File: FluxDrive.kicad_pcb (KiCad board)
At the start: 4 copper layers, 60 x 54.5 mm, 124 parts, among them J1 Amiga floppy 34, J2 Floppy power, J3 USB-C, J4 UART / recovery, J5 Spare GPIO, SW1 BOOT, SW2 RESET, U1 ESP32-S3-WROOM-1-N16R8, U2 74LVC14A, U3 74LVC14A, U4 74LVC07A, U5 TPS259531, U6 TLV62569DBVR, U7 USBLC6-2SC6

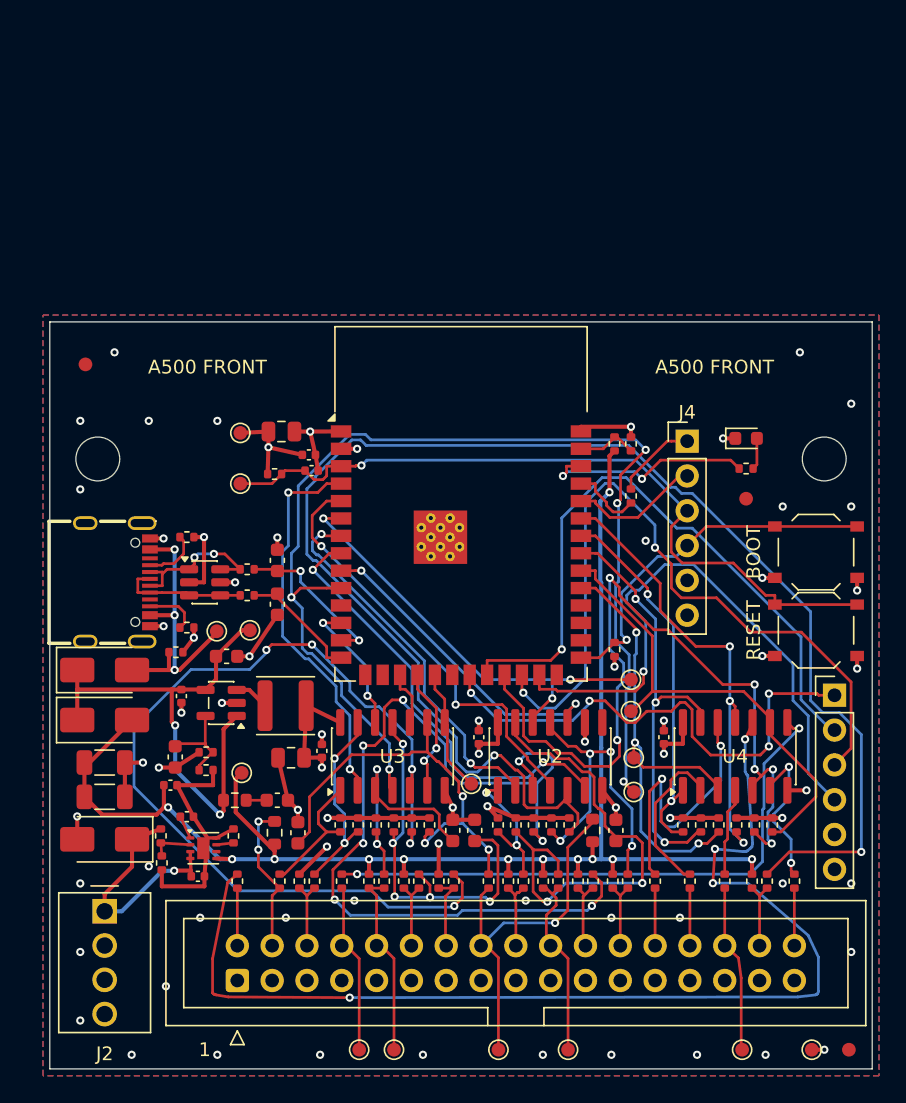
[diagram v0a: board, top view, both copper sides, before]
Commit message: Rev B placement: J6 beside J1, 72.1 mm, every part found by net (unrouted)
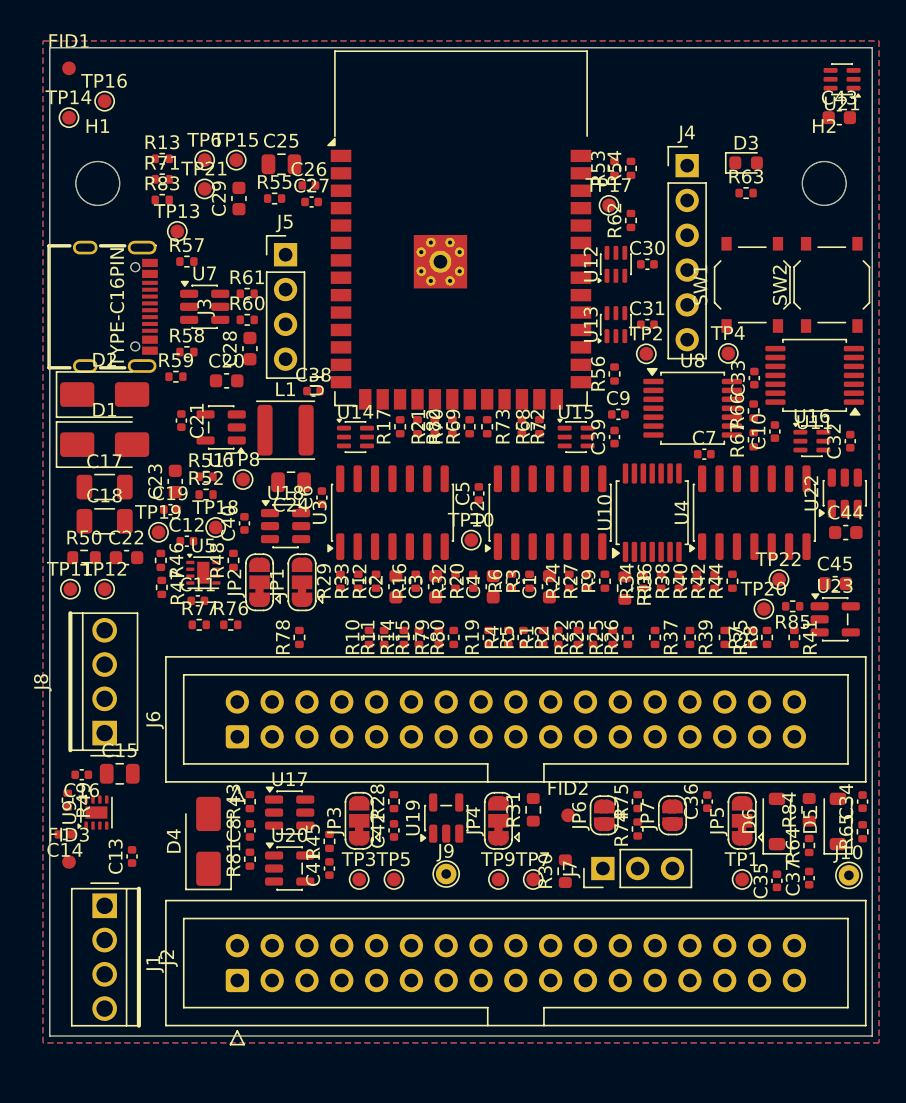
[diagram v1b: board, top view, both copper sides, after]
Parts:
- added C23: 15pF, Capacitor_SMD:C_0603_1608Metric, F.Cu at (109.2, 105.1)
- added C24: 22uF, Capacitor_SMD:C_0805_2012Metric, F.Cu at (117.6, 105.2)
- added C25: 22uF, Capacitor_SMD:C_0805_2012Metric, F.Cu at (116.9, 82.0)
- added C26: 100nF, Capacitor_SMD:C_0402_1005Metric, F.Cu at (118.9, 83.5)
- added C27: 1uF, Capacitor_SMD:C_0402_1005Metric, F.Cu at (119.1, 84.8)
- added C28: 10pF, Capacitor_SMD:C_0603_1608Metric, F.Cu at (114.6, 95.5)
- added C29: 10pF, Capacitor_SMD:C_0603_1608Metric, F.Cu at (113.8, 84.5)
- added C30: 100nF, Capacitor_SMD:C_0402_1005Metric, F.Cu at (143.6, 89.3)
- added C31: 100nF, Capacitor_SMD:C_0402_1005Metric, F.Cu at (143.6, 93.7)
- added C32: 100nF, Capacitor_SMD:C_0402_1005Metric, F.Cu at (158.4, 102.2)
- added C33: 100nF, Capacitor_SMD:C_0402_1005Metric, F.Cu at (151.4, 97.6)
- added C34: 1uF, Capacitor_SMD:C_0402_1005Metric, F.Cu at (159.3, 128.5)
- added C35: 1uF, Capacitor_SMD:C_0402_1005Metric, F.Cu at (153.1, 134.3)
- added C36: 100nF, Capacitor_SMD:C_0402_1005Metric, F.Cu at (148.0, 128.5)
- added C37: 100nF, Capacitor_SMD:C_0402_1005Metric, F.Cu at (155.4, 134.1)
- added C38: 100nF, Capacitor_SMD:C_0402_1005Metric, F.Cu at (119.2, 98.5)
- added C39: 100nF, Capacitor_SMD:C_0402_1005Metric, F.Cu at (141.2, 101.9)
- added C40: 100nF, Capacitor_SMD:C_0402_1005Metric, F.Cu at (114.2, 108.2)
- added C41: 100nF, Capacitor_SMD:C_0402_1005Metric, F.Cu at (120.4, 133.4)
- added C42: 100nF, Capacitor_SMD:C_0402_1005Metric, F.Cu at (125.1, 130.6)
- added C43: 100nF, Capacitor_SMD:C_0603_1608Metric, F.Cu at (157.6, 78.6)
- added C44: 100nF, Capacitor_SMD:C_0603_1608Metric, F.Cu at (158.1, 108.9)
- added C45: 100nF, Capacitor_SMD:C_0603_1608Metric, F.Cu at (157.3, 112.6)
- added D5: 1N4148W, Diode_SMD:D_SOD-123, F.Cu at (157.5, 129.9)
- added D6: 1N4148W, Diode_SMD:D_SOD-123, F.Cu at (153.1, 129.9)
- added J10: MTRX wire, TestPoint:TestPoint_THTPad_D1.5mm_Drill0.7mm, F.Cu at (158.3, 133.9)
- added J6: Original drive, Connector_IDC:IDC-Header_2x17_P2.54mm_Vertical, F.Cu at (113.7, 123.8)
- added J7: DF0 switch, Connector_PinHeader_2.54mm:PinHeader_1x03_P2.54mm_Vertical, F.Cu at (140.3, 133.4)
- added J8: Drive power, FluxDrive:171825-4, F.Cu at (104.0, 123.5)
- added J9: RST wire, TestPoint:TestPoint_THTPad_D1.5mm_Drill0.7mm, F.Cu at (128.9, 133.8)
- added JP1: bypass SEL, Jumper:SolderJumper-3_P1.3mm_Bridged12_RoundedPad1.0x1.5mm, F.Cu at (118.4, 112.5)
- added JP2: bypass MTR, Jumper:SolderJumper-3_P1.3mm_Bridged12_RoundedPad1.0x1.5mm, F.Cu at (115.3, 112.5)
- added JP3: mode 4 SEL, Jumper:SolderJumper-3_P1.3mm_Bridged12_RoundedPad1.0x1.5mm, F.Cu at (122.6, 129.9)
- added JP4: mode 4 MTR, Jumper:SolderJumper-3_P1.3mm_Bridged12_RoundedPad1.0x1.5mm, F.Cu at (132.7, 129.9)
- added JP5: DF0 at power-on, Jumper:SolderJumper-3_P1.3mm_Bridged12_RoundedPad1.0x1.5mm, F.Cu at (150.5, 129.9)
- added JP6: REAL clear, Jumper:SolderJumper-2_P1.3mm_Open_RoundedPad1.0x1.5mm, F.Cu at (140.4, 129.5)
- added JP7: REAL preset, Jumper:SolderJumper-2_P1.3mm_Open_RoundedPad1.0x1.5mm, F.Cu at (145.4, 129.5)
- added R63: 1K, Resistor_SMD:R_0402_1005Metric, F.Cu at (150.8, 84.1)
- added R64: 10K, Resistor_SMD:R_0402_1005Metric, F.Cu at (155.4, 131.7)
- added R65: 10K, Resistor_SMD:R_0402_1005Metric, F.Cu at (159.3, 130.7)
- added R66: 10K, Resistor_SMD:R_0402_1005Metric, F.Cu at (151.3, 100.0)
- added R67: 10K, Resistor_SMD:R_0402_1005Metric, F.Cu at (151.3, 102.1)
- added R68: 100K, Resistor_SMD:R_0402_1005Metric, F.Cu at (135.7, 101.2)
- added R69: 100K, Resistor_SMD:R_0402_1005Metric, F.Cu at (130.6, 101.2)
- added R70: 1K, Resistor_SMD:R_0402_1005Metric, F.Cu at (129.4, 101.2)
- added R71: 1K, Resistor_SMD:R_0402_1005Metric, F.Cu at (108.2, 83.1)
- added R72: 10K, Resistor_SMD:R_0402_1005Metric, F.Cu at (134.4, 101.2)
- added R73: 10K, Resistor_SMD:R_0402_1005Metric, F.Cu at (131.9, 101.2)
- added R74: 1K, Resistor_SMD:R_0402_1005Metric, F.Cu at (142.9, 130.5)
- added R75: 1K, Resistor_SMD:R_0402_1005Metric, F.Cu at (142.9, 128.5)
- added R76: 4K7, Resistor_SMD:R_0402_1005Metric, F.Cu at (113.2, 115.6)
- added R77: 4K7, Resistor_SMD:R_0402_1005Metric, F.Cu at (110.9, 115.6)
- added R78: 10K, Resistor_SMD:R_0402_1005Metric, F.Cu at (118.2, 116.5)
- added R79: 10K, Resistor_SMD:R_0402_1005Metric, F.Cu at (128.4, 116.5)
- added R80: 10K, Resistor_SMD:R_0402_1005Metric, F.Cu at (129.5, 116.5)
- added R81: 33, Resistor_SMD:R_0402_1005Metric, F.Cu at (114.6, 132.7)
- added R82: 10K, Resistor_SMD:R_0402_1005Metric, F.Cu at (126.8, 101.2)
- added R83: 1K, Resistor_SMD:R_0402_1005Metric, F.Cu at (108.2, 84.6)
- added R84: 33, Resistor_SMD:R_0603_1608Metric, F.Cu at (155.4, 129.1)
- added R85: 100K, Resistor_SMD:R_0402_1005Metric, F.Cu at (154.2, 114.2)
- added TP17: SEL_FD, TestPoint:TestPoint_Pad_D1.0mm, F.Cu at (140.8, 85.0)
- added TP18: REAL_SEL, TestPoint:TestPoint_Pad_D1.0mm, F.Cu at (112.1, 108.5)
- added TP19: REAL_MTR, TestPoint:TestPoint_Pad_D1.0mm, F.Cu at (107.9, 108.8)
- added TP20: DF0_FD, TestPoint:TestPoint_Pad_D1.0mm, F.Cu at (152.1, 114.5)
- added TP21: DF1_EN, TestPoint:TestPoint_Pad_D1.0mm, F.Cu at (111.3, 83.8)
- added TP22: MODE_CLK, TestPoint:TestPoint_Pad_D1.0mm, F.Cu at (153.2, 112.3)
- added U10: 74LVC32A, Package_SO:TSSOP-14_4.4x5mm_P0.65mm, F.Cu at (143.9, 107.4)
- added U11: 74LVC32A, Package_SO:TSSOP-14_4.4x5mm_P0.65mm, F.Cu at (155.8, 97.4)
- added U12: 74LVC1G157, Package_TO_SOT_SMD:SOT-363_SC-70-6, F.Cu at (141.3, 89.3)
- added U13: 74LVC1G157, Package_TO_SOT_SMD:SOT-363_SC-70-6, F.Cu at (141.3, 93.7)
- added U14: 74LVC1G157, Package_TO_SOT_SMD:SOT-363_SC-70-6, F.Cu at (122.3, 101.9)
- added U15: 74LVC1G157, Package_TO_SOT_SMD:SOT-363_SC-70-6, F.Cu at (138.4, 101.9)
- added U16: 74LVC1G157, Package_TO_SOT_SMD:SOT-363_SC-70-6, F.Cu at (155.6, 102.2)
- added U17: SN74LVC2G07, Package_TO_SOT_SMD:SOT-23-6, F.Cu at (117.5, 129.3)
- added U18: SN74LVC2G06, Package_TO_SOT_SMD:SOT-23-6, F.Cu at (117.2, 108.4)
- added U19: SN74LVC1G06, Package_TO_SOT_SMD:SOT-23-5, F.Cu at (128.9, 129.7)
- added U20: SN74LVC1G38, Package_TO_SOT_SMD:SOT-23-5, F.Cu at (117.5, 133.4)
- added U21: 74LVC1G157, Package_TO_SOT_SMD:SOT-363_SC-70-6, F.Cu at (157.8, 75.8)
- added U22: SN74LVC1G175, Package_TO_SOT_SMD:SOT-23-6, F.Cu at (158.0, 106.0)
- added U23: SN74LVC1G38, Package_TO_SOT_SMD:SOT-23-5, F.Cu at (157.3, 115.2)
- added U8: 74LVC74A, Package_SO:TSSOP-14_4.4x5mm_P0.65mm, F.Cu at (146.9, 99.8)
- added U9: TPS259531, Package_SON:Texas_DSG0008A_WSON-8-1EP_2x2mm_P0.5mm_EP0.9x1.6mm, F.Cu at (103.4, 129.3)
- C10: value 47uF -> 100nF; footprint Capacitor_SMD:C_1206_3216Metric -> Capacitor_SMD:C_0402_1005Metric
- C11: value 47uF -> 1uF; footprint Capacitor_SMD:C_1206_3216Metric -> Capacitor_SMD:C_0402_1005Metric
- C12, C14: value 100nF -> 22nF
- C13: value 10uF -> 1uF; footprint Capacitor_SMD:C_0603_1608Metric -> Capacitor_SMD:C_0402_1005Metric
- C15: value 4.7uF -> 22uF; footprint Capacitor_SMD:C_0603_1608Metric -> Capacitor_SMD:C_0805_2012Metric
- C16: value 15pF -> 100nF; footprint Capacitor_SMD:C_0603_1608Metric -> Capacitor_SMD:C_0402_1005Metric
- C17, C18: value 22uF -> 47uF; footprint Capacitor_SMD:C_0805_2012Metric -> Capacitor_SMD:C_1206_3216Metric
- C20: value 1uF -> 10uF; footprint Capacitor_SMD:C_0402_1005Metric -> Capacitor_SMD:C_0603_1608Metric
- C21: value 10pF -> 100nF; footprint Capacitor_SMD:C_0603_1608Metric -> Capacitor_SMD:C_0402_1005Metric
- C22: value 10pF -> 4.7uF
- C8: value 1uF -> 100nF
- C9: value 22nF -> 100nF
- J5: value Spare GPIO -> Spare / OLED; footprint Connector_PinHeader_2.54mm:PinHeader_1x06_P2.54mm_Vertical -> Connector_PinHeader_2.54mm:PinHeader_1x04_P2.54mm_Vertical
- R1, R4, R7: value 1K -> 4K7
- R13: value 10K -> 1K
- R14, R17: value 100 -> 1K
- R15: value 100K -> 100
- R16: value 1K -> 100K; footprint Resistor_SMD:R_0603_1608Metric -> Resistor_SMD:R_0402_1005Metric
- R18: value 100K -> 1K; footprint Resistor_SMD:R_0402_1005Metric -> Resistor_SMD:R_0603_1608Metric
- R19: value 4K7 -> 100
- R20, R29, R32: value 100 -> 100K
- R21: value 100K -> 1K
- R25: value 1K -> 4K7; footprint Resistor_SMD:R_0603_1608Metric -> Resistor_SMD:R_0402_1005Metric
- R28: value 10K -> 100
- R30: value 100K -> 4K7; footprint Resistor_SMD:R_0402_1005Metric -> Resistor_SMD:R_0603_1608Metric
- R31: value 10K -> 100; footprint Resistor_SMD:R_0402_1005Metric -> Resistor_SMD:R_0603_1608Metric
- R49: value 1R -> 1K37; footprint Resistor_SMD:R_0603_1608Metric -> Resistor_SMD:R_0402_1005Metric
- R50: value 100K -> 1R; footprint Resistor_SMD:R_0402_1005Metric -> Resistor_SMD:R_0603_1608Metric
- R51: value 22K -> 100K
- R52: value 1K -> 22K
- R53: value 1K5 -> 1K
- R54: value 10K -> 1K5
- R56: value 5K1 -> 10K
- R58: value 10K -> 5K1
- R59: value 22 -> 10K
- R61: value 470 -> 22
- R62: value 1K -> 470
- moved TP16 86.3 mm to (104.0, 77.4)
- moved FID3 58.5 mm to (101.4, 132.9)
- moved TP6 55.7 mm to (111.3, 81.7)
- moved R13 55.6 mm to (108.2, 81.6), turned to 0 degrees
- moved C10 54.5 mm to (152.9, 101.5), turned to 90 degrees
- moved J5 51.4 mm to (117.2, 88.6)
- moved C9 43.0 mm to (141.5, 100.2)
- moved R55 41.2 mm to (116.4, 84.5), turned to 0 degrees
- moved R54 34.3 mm to (142.4, 82.3), turned to 90 degrees
- moved R45 34.0 mm to (120.4, 131.4), turned to 90 degrees
- moved R17 33.8 mm to (125.6, 101.2)
- moved R56 33.4 mm to (141.2, 97.3), turned to 90 degrees
- moved TP8 31.8 mm to (114.1, 105.0)
- moved R61 31.6 mm to (114.4, 91.5), turned to 0 degrees
- moved R26 31.0 mm to (142.2, 116.5)
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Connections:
- C10 pad 1: /+5V_A -> /+3V3
- C11 pad 1: /+5V_A -> /+5V_IN
- C12 pad 1: /+5V_A -> /EFUSE_DVDT
- C13 pad 1: /V5SYS -> /+5V_IN
- C14 pad 1: /V5SYS -> /DRV_DVDT
- C15 pad 1: /V5SYS_DAMP -> /+5V_DRIVE
- C16 pad 1: /+3V3 -> /+5V_DRIVE
- C16 pad 2: /BUCK_FB -> /GND
- C17 pad 1: /+3V3 -> /+5V_A
- C18 pad 1: /+3V3 -> /+5V_A
- C19 pad 1: /+3V3 -> /+5V_A
- C20 pad 1: /ESP_EN -> /V5SYS
- C21 pad 1: /USB_DP -> /V5SYS
- C22 pad 1: /USB_DN -> /V5SYS_DAMP
- C8 pad 1: /+5V_IN -> /+3V3
- C9 pad 1: /EFUSE_DVDT -> /+3V3
- J1 pad 14: /FD_PIN14 -> unconnected-(J1-Pin_14-Pad14)
- J1 pad 4: /_MTR0_P4 -> unconnected-(J1-Pin_4-Pad4)
- J1 pad 6: /FD_PIN6 -> unconnected-(J1-Pin_6-Pad6)
- J2 pad 4: unconnected-(J2-12V-Pad4) -> /+12V
- J5 pad 1: /GPIO13 -> /GND
- J5 pad 2: /GPIO14 -> /+3V3
- J5 pad 3: /GPIO47 -> /GPIO18
- J5 pad 4: /GPIO48 -> /GPIO3
- R13 pad 1: /_SEL1 -> /SEL0
- R13 pad 2: /+5V_A -> /SEL0_IO
- R14 pad 2: /SEL1_B -> /+5V_A
- R15 pad 1: /SEL1_B -> /_SEL1
- R15 pad 2: /+3V3 -> /SEL1_B
- R16 pad 1: /_MTR0 -> /SEL1_B
- R16 pad 2: /+5V_A -> /+3V3
- R17 pad 1: /_MTR0 -> /SEL1
- R17 pad 2: /MTR0_B -> /SEL1_IO
- R18 pad 1: /MTR0_B -> /_MTR0
- R18 pad 2: /+3V3 -> /+5V_A
- R19 pad 1: /_DKWD -> /_MTR0
- R19 pad 2: /+5V_A -> /MTR0_B
- R20 pad 1: /_DKWD -> /MTR0_B
- R20 pad 2: /DKWD_B -> /+3V3
- R21 pad 1: /DKWD_B -> /MTR0
- R21 pad 2: /+3V3 -> /MTR0_IO
- R22 pad 1: /_DKWE -> /_DKWD
- R23 pad 1: /_DKWE -> /_DKWD
- R23 pad 2: /DKWE_B -> /DKWD_B
- R24 pad 1: /DKWE_B -> /DKWD_B
- R25 pad 1: /_MTR0_P4 -> /_DKWE
- R26 pad 1: /_MTR0_P4 -> /_DKWE
- R26 pad 2: /MTR0_P4_B -> /DKWE_B
- R27 pad 1: /MTR0_P4_B -> /DKWE_B
- R28 pad 1: /FD_PIN6 -> /KBRESET
- R28 pad 2: /+3V3 -> /RST_B
- R29 pad 1: /FD_PIN6 -> /RST_B
- R29 pad 2: /PIN6_B -> /+3V3
- R30 pad 1: /PIN6_B -> /MTRX
- R30 pad 2: /+3V3 -> /+5V_A
- R31 pad 1: /FD_PIN14 -> /MTRX
- R31 pad 2: /+3V3 -> /MTRX_B
- R32 pad 1: /FD_PIN14 -> /MTRX_B
- R32 pad 2: /PIN14_B -> /+3V3
- R33 pad 1: /PIN14_B -> /M4_MTR_Q
- R33 pad 2: /+3V3 -> /GND
- R36 pad 1: /INDEX_N -> /TRK0_N
- R37 pad 1: /INDEX_D -> /TRK0_D
- R37 pad 2: /_INDEX -> /_TRK0
- R38 pad 1: /TRK0_N -> /WPROT_N
- R39 pad 1: /TRK0_D -> /WPROT_D
- R39 pad 2: /_TRK0 -> /_WPROT
- R40 pad 1: /WPROT_N -> /RDY_N
- R41 pad 1: /WPROT_D -> /RDY_D
- R41 pad 2: /_WPROT -> /_RDY
- R44 pad 1: /RDY_N -> /INDEX_N
- R45 pad 1: /RDY_D -> /INDEX_D
- R45 pad 2: /_RDY -> /_INDEX
- R49 pad 1: /V5SYS -> /DRV_ILM
- R49 pad 2: /V5SYS_DAMP -> /GND
- R50 pad 1: /+3V3 -> /V5SYS
- R50 pad 2: /BUCK_FB -> /V5SYS_DAMP
- R51 pad 1: /BUCK_FB -> /+3V3
- R51 pad 2: /GND -> /BUCK_FB
- R52 pad 1: /+5V_A -> /BUCK_FB
- R52 pad 2: /AMIGA_PWR -> /GND
- R53 pad 1: /AMIGA_PWR -> /+5V_A
- R53 pad 2: /GND -> /AMIGA_PWR
- R54 pad 1: /+3V3 -> /AMIGA_PWR
- R54 pad 2: /ESP_EN -> /GND
- R55 pad 2: /BOOT -> /ESP_EN
- R56 pad 1: /USB_CC1 -> /+3V3
- R56 pad 2: /GND -> /BOOT
- R57 pad 1: /USB_CC2 -> /USB_CC1
- R58 pad 1: /VBUS -> /USB_CC2
- R59 pad 1: /USB_DP_C -> /VBUS
- R59 pad 2: /USB_DP -> /GND
- R60 pad 1: /USB_DN_C -> /USB_DP_C
- R60 pad 2: /USB_DN -> /USB_DP
- R61 pad 1: /ESP_TXD0 -> /USB_DN_C
- R61 pad 2: /UART_TX -> /USB_DN
- R62 pad 1: /LED -> /ESP_TXD0
- R62 pad 2: /LED_A -> /UART_TX
- U1 pad 10: /SEL0 -> /SEL0_IO
- U1 pad 11: unconnected-(U1-IO18-Pad11) -> /GPIO18
- U1 pad 12: /PIN6 -> /DF1_STATE
- U1 pad 15: unconnected-(U1-IO3-Pad15) -> /GPIO3
- U1 pad 17: /SEL1 -> /SEL1_IO
- U1 pad 18: /PIN14 -> /RST_REQ
- U1 pad 19: /MTR0 -> /MTR0_IO
- U1 pad 20: unconnected-(U1-IO12-Pad20) -> /DF0_STATE
- U1 pad 21: /GPIO13 -> /DF1_REQ
- U1 pad 22: /GPIO14 -> /CHNG_REQ
- U1 pad 24: /GPIO47 -> /MODE_CLK_REQ
- U1 pad 25: /GPIO48 -> /DF0_REQ
- U1 pad 4: /MTR0_P4 -> /RST_ACT_IO
- U2 pad 8: unconnected-(U2-Pad8) -> /SEL_FD_N
- U2 pad 9: /GND -> /SEL_FD
- U3 pad 1: /MTR0_P4_B -> /RST_B
- U3 pad 12: /PIN6 -> /M4_MTR_N
- U3 pad 13: /PIN6_B -> /M4_MTR_Q
- U3 pad 2: /MTR0_P4 -> /RST_ACT
- U3 pad 5: /PIN14_B -> /MTRX_B
- U3 pad 6: /PIN14 -> /M4_MOTOR
- U4 pad 1: /WPROT_N -> /WPROT_G
- U4 pad 10: /CHNG_D -> unconnected-(U4-Pad10)
- U4 pad 11: /CHNG_N -> /+3V3
- U4 pad 13: /TRK0_N -> /TRK0_G
- U4 pad 3: /DKRD_N -> /DKRD_G
- U4 pad 5: /RDY_N -> /RDY_G
- U4 pad 8: /INDEX_D -> unconnected-(U4-Pad8)
- U4 pad 9: /INDEX_N -> /+3V3
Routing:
- net /SIDE_B: track 111.0 -> 0.00 mm, vias 2 -> 0
- net /+5V_A: track 108.4 -> 0.00 mm, vias 12 -> 0
- net /SEL0: track 83.8 -> 0.00 mm, vias 5 -> 0
- net /CHNG_D: track 80.8 -> 0.00 mm, vias 4 -> 0
- net /GND: track 73.2 -> 0.00 mm, vias 58 -> 0
- net /PIN14_B: track 70.5 -> 0.00 mm, vias 5 -> 0
- net /DKWD_B: track 66.6 -> 0.00 mm, vias 7 -> 0
- net /+3V3: track 66.3 -> 0.00 mm, vias 14 -> 0
- net /RDY_N: track 57.6 -> 0.00 mm, vias 6 -> 0
- net /ESP_EN: track 54.8 -> 0.00 mm, vias 1 -> 0
- net /GPIO47: track 54.5 -> 0.00 mm, vias 2 -> 0
- net /GPIO14: track 47.9 -> 0.00 mm, vias 1 -> 0
- net /GPIO48: track 43.2 -> 0.00 mm, vias 1 -> 0
- net /INDEX_D: track 43.0 -> 0.00 mm, vias 2 -> 0
- net /GPIO13: track 37.6 -> 0.00 mm, vias 4 -> 0
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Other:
- board size 60 x 54.5 mm -> 60 x 72.1 mm
- board text removed: "+5V"
- board text removed: "1"
- board text removed: "12V nc"
- board text removed: "3V3"
- board text removed: "40 mm"
- board text removed: "50 mm"
- board text removed: "A500 FRONT"
- board text removed: "BOOT"
- board text removed: "EN"
- board text removed: "FluxDrive v1 rev A"
- board text removed: "GND"
- board text removed: "IO0"
- board text removed: "IO13"
- board text removed: "IO14"
- board text removed: "IO47"
- board text removed: "IO48"
- board text removed: "J1 option: 2x17 female socket on this side,"
- board text removed: "JLCJLCJLCJLC"
- board text removed: "RESET"
- board text removed: "RX"
- board text removed: "S/N"
- board text removed: "TX"
- board text removed: "UART"
- board text removed: "by Dimmy (Dimitri Hilverda)"
- board text removed: "plugs onto the A500 header. Pin 1 = square pad"
- board text removed: "print at 100 %: both bars must measure exactly 50 mm / 40 mm"
